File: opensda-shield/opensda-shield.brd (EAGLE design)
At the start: 21.6 x 53.3 mm, 17 parts, among them IC1 74LVC125, IC2 74LVC125, J1 61302011121, J2 61302011121, J3 61300211121, J4 CORTEX_DEBUG_PTH, J5 61301511121

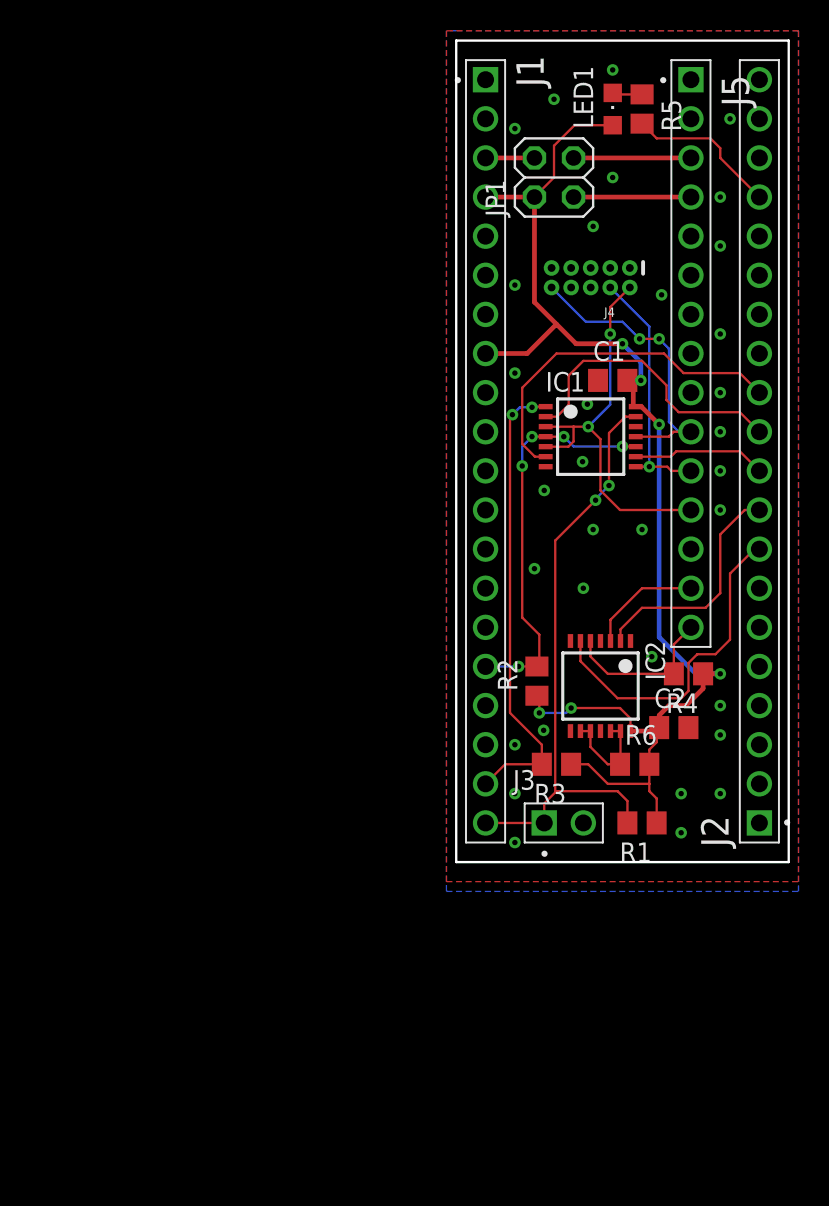
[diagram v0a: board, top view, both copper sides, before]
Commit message: Premisten J4 a prehozeny gaty bufferu
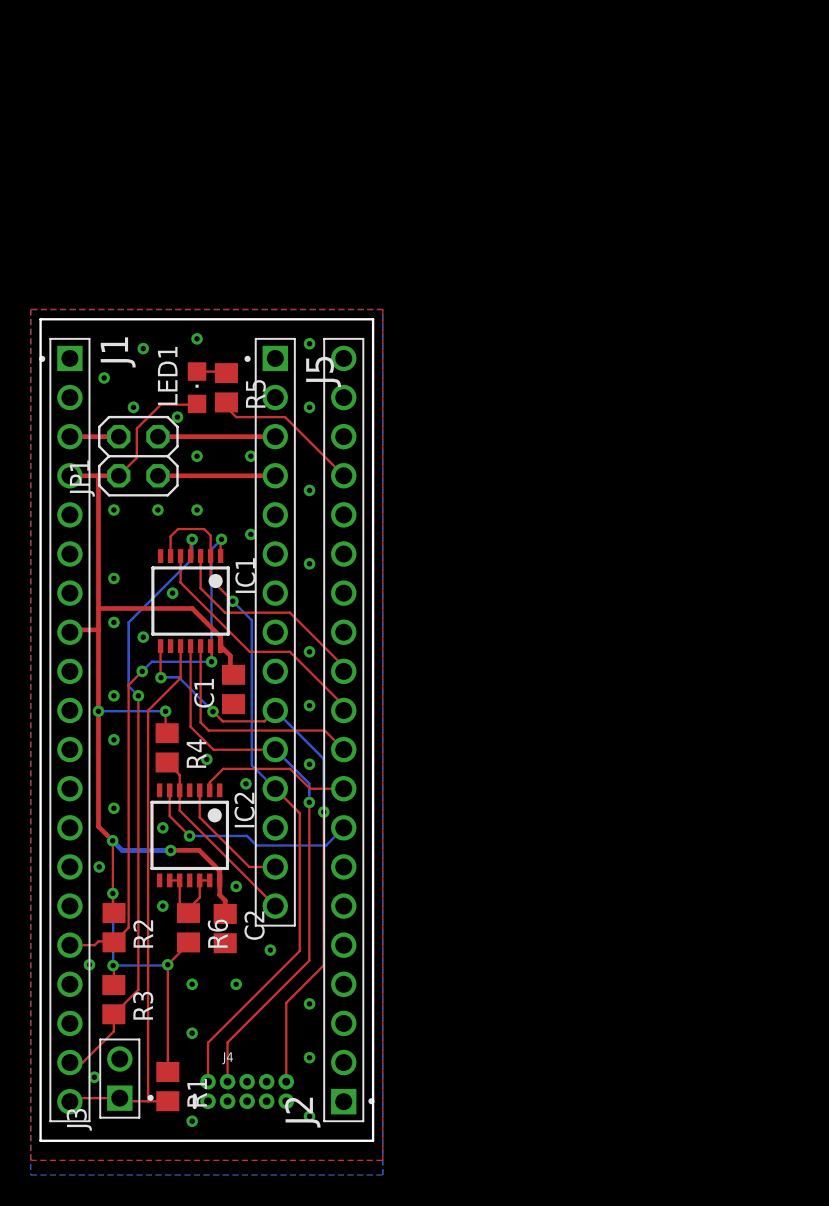
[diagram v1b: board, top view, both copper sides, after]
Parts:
- moved J4 57.4 mm to (16.3, 6.69), turned to 0 degrees
- moved R1 35.2 mm to (11.1, 7.01), turned to 270 degrees
- moved R4 34.2 mm to (11.1, 29.0), turned to 270 degrees
- moved J3 33.3 mm to (8.00, 7.53), turned to 90 degrees
- moved R3 32.6 mm to (7.61, 12.7), turned to 270 degrees
- moved J1 32.5 mm to (4.76, 30.2)
- moved J2 32.5 mm to (22.5, 30.2)
- moved J5 32.5 mm to (18.1, 36.5)
- moved JP1 32.5 mm to (9.21, 47.9)
- moved LED1 32.5 mm to (13.0, 52.4)
- moved R5 32.5 mm to (14.9, 52.4)
- moved C2 31.9 mm to (14.8, 17.3), turned to 270 degrees
- moved R2 31.8 mm to (7.63, 17.3), turned to 270 degrees
- moved C1 31.8 mm to (15.4, 32.8), turned to 90 degrees
- moved R6 30.9 mm to (12.5, 17.3), turned to 270 degrees
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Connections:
- net GND: now also IC1.9; no longer IC1.12
- net PTA4: now also IC1.1, IC1.13; no longer IC1.10, IC1.4
- net PTB0: now also IC1.4; no longer IC1.1
- net PTB1: now also IC1.10; no longer IC1.13
- net PTC5: now also IC1.12; no longer IC1.9
- net PTC6: now also IC1.5; no longer IC1.2
- net PTC7: now also IC1.3; no longer IC1.6
- net RST_TGT: now also IC1.8; no longer IC1.11
- net SWD_CLK_TGT: now also IC1.11; no longer IC1.8
- net SWD_DIO_TGT: now also IC1.2, IC1.6; no longer IC1.3, IC1.5
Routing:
- net SWD_CLK_TGT: track 16.4 -> 36.0 mm
- net RST_TGT: track 19.4 -> 37.4 mm, vias 2 -> 3
- net SWD_DIO_TGT: track 27.0 -> 44.6 mm, vias 2 -> 1
- net PTA4: track 26.1 -> 36.5 mm, vias 5 -> 3
- net PTB0: track 30.2 -> 39.5 mm
- net PTC7: track 22.9 -> 13.8 mm
- net PTC3: track 21.5 -> 14.2 mm, vias 0 -> 1
- net PTC5: track 8.70 -> 15.0 mm
- net PTC4: track 15.2 -> 10.1 mm
- net PTC6: track 19.0 -> 15.9 mm
- net 3V3: track 85.7 -> 88.6 mm, vias 6 -> 7
- net PTB1: track 39.5 -> 37.0 mm, vias 2 -> 0
- net TX_TGT: track 10.4 -> 12.2 mm
- net N$5: track 6.88 -> 6.11 mm
- net RX_TGT: track 7.45 -> 8.00 mm

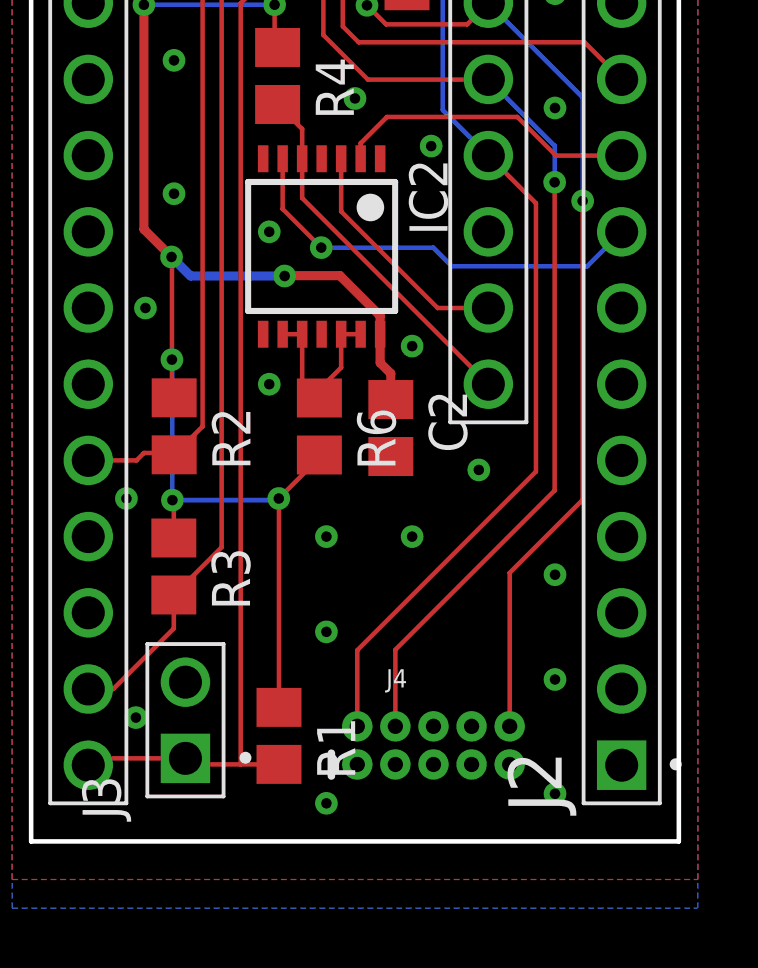
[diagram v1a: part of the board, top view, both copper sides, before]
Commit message: Posunuti J4
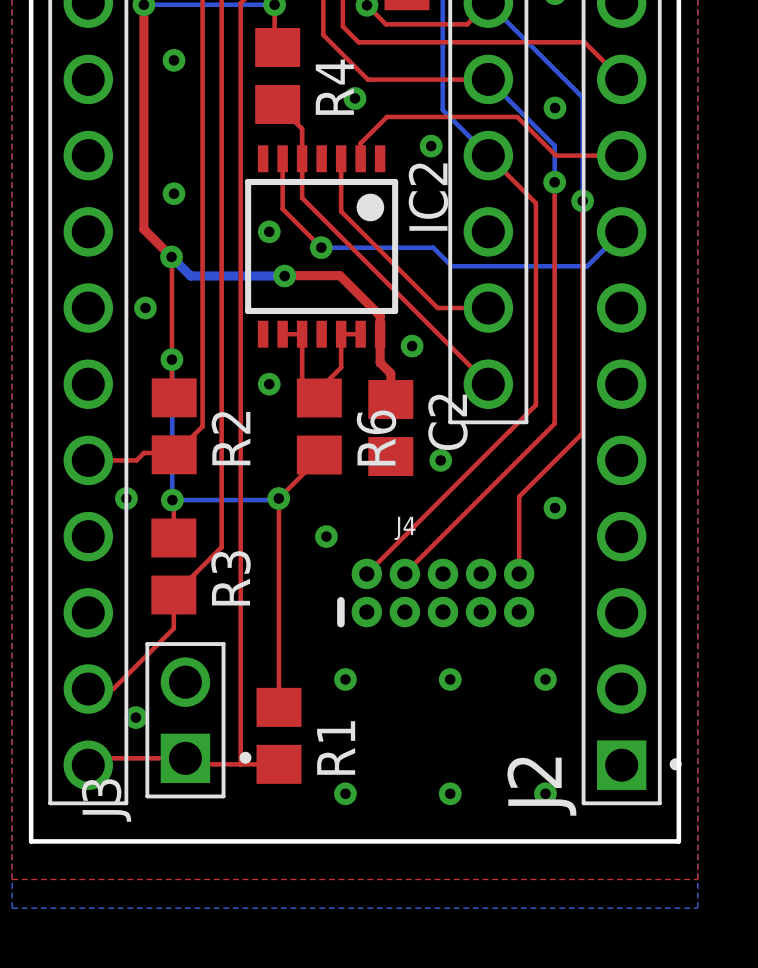
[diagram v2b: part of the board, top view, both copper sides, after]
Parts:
- moved J4 5.09 mm to (16.6, 11.8)
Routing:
- net SWD_CLK_TGT: track 36.0 -> 30.8 mm
- net RST_TGT: track 37.4 -> 32.2 mm
- net SWD_DIO_TGT: track 44.6 -> 39.4 mm
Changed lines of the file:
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@@
 <attribute name="VALUE" x="11.684" y="4.2291" size="1.27" layer="27" rot="R90"/>
 </element>
-<element name="J4" library="SparkFun-Connectors" library_urn="urn:adsk.eagle:library:513" package="2X5-PTH-1.27MM" package3d_urn="urn:adsk.eagle:package:38290/1" value="CORTEX_DEBUG_PTH" x="16.2687" y="6.6929" smashed="yes">
-<attribute name="NAME" x="14.6939" y="8.6233" size="0.6096" layer="25" font="vector" ratio="20"/>
-<attribute name="VALUE" x="14.4399" y="4.2291" size="0.6096" layer="27" font="vector" ratio="20"/>
+<element name="J4" library="SparkFun-Connectors" library_urn="urn:adsk.eagle:library:513" package="2X5-PTH-1.27MM" package3d_urn="urn:adsk.eagle:package:38290/1" value="CORTEX_DEBUG_PTH" x="16.5862" y="11.7729" smashed="yes">
+<attribute name="NAME" x="15.0114" y="13.7033" size="0.6096" layer="25" font="vector" ratio="20"/>
+<attribute name="VALUE" x="14.7574" y="9.3091" size="0.6096" layer="27" font="vector" ratio="20"/>
 </element>
 <element name="J5" library="Headers" library_urn="urn:adsk.eagle:library:11687645" package="61301511121" package3d_urn="urn:adsk.eagle:package:11391913/2" value="61301511121" x="18.0975" y="36.5125" smashed="yes" rot="R270">
@@
 <contactref element="IC1" pad="9"/>
 <via x="12.7" y="13.6525" extent="1-16" drill="0.35"/>
-<via x="17.78" y="15.875" extent="1-16" drill="0.35"/>
-<via x="15.5575" y="13.6525" extent="1-16" drill="0.35"/>
-<via x="12.7" y="10.4775" extent="1-16" drill="0.35"/>
-<via x="20.32" y="12.3825" extent="1-16" drill="0.35"/>
-<via x="20.32" y="8.89" extent="1-16" drill="0.35"/>
-<via x="20.32" y="5.08" extent="1-16" drill="0.35"/>
-<via x="12.7" y="4.7625" extent="1-16" drill="0.35"/>
+<via x="16.51" y="16.1925" extent="1-16" drill="0.35"/>
+<via x="16.8275" y="8.89" extent="1-16" drill="0.35"/>
+<via x="13.335" y="8.89" extent="1-16" drill="0.35"/>
+<via x="20.0025" y="5.08" extent="1-16" drill="0.35"/>
+<via x="20.0025" y="8.89" extent="1-16" drill="0.35"/>
+<via x="16.8275" y="5.08" extent="1-16" drill="0.35"/>
+<via x="13.335" y="5.08" extent="1-16" drill="0.35"/>
 <via x="6.35" y="7.62" extent="1-16" drill="0.35"/>
 <via x="6.0325" y="14.9225" extent="1-16" drill="0.35"/>
@@
 <via x="10.795" y="23.8125" extent="1-16" drill="0.35"/>
 <via x="10.795" y="18.7325" extent="1-16" drill="0.35"/>
+<via x="20.32" y="14.605" extent="1-16" drill="0.35"/>
 </signal>
 <signal name="VIN">
@@
 <wire x1="16.57985" y1="27.87015" x2="18.0975" y2="26.3525" width="0.1524" layer="16"/>
 <wire x1="16.57985" y1="37.2872" x2="16.57985" y2="27.87015" width="0.1524" layer="16"/>
-<wire x1="13.7287" y1="7.3279" x2="13.7287" y2="9.86155" width="0.1524" layer="1"/>
+<wire x1="18.81505" y1="17.1704" x2="18.8087" y2="17.1704" width="0.1524" layer="1"/>
+<wire x1="18.8087" y1="17.1704" x2="14.0462" y2="12.4079" width="0.1524" layer="1"/>
 <wire x1="19.685" y1="24.765" x2="18.0975" y2="26.3525" width="0.1524" layer="1"/>
-<wire x1="13.7287" y1="9.86155" x2="19.685" y2="15.81785" width="0.1524" layer="1"/>
-<wire x1="19.685" y1="15.81785" x2="19.685" y2="24.765" width="0.1524" layer="1"/>
+<wire x1="18.81505" y1="17.1704" x2="19.685" y2="18.04035" width="0.1524" layer="1"/>
+<wire x1="19.685" y1="18.04035" x2="19.685" y2="24.765" width="0.1524" layer="1"/>
 <wire x1="13.48105" y1="43.21175" x2="11.77925" y2="43.21175" width="0.1524" layer="1"/>
 <wire x1="11.2984" y1="42.7309" x2="11.2984" y2="41.46315" width="0.1524" layer="1"/>
@@
 <wire x1="18.09115" y1="28.88615" x2="14.0843" y2="28.88615" width="0.1524" layer="1"/>
 <wire x1="12.5984" y1="30.37205" x2="14.0843" y2="28.88615" width="0.1524" layer="1"/>
-<wire x1="14.9987" y1="7.3279" x2="14.9987" y2="9.8806" width="0.1524" layer="1"/>
-<wire x1="20.3073" y1="15.1892" x2="20.3073" y2="25.4635" width="0.1524" layer="1"/>
+<wire x1="20.3073" y1="17.4117" x2="20.3073" y2="25.4635" width="0.1524" layer="1"/>
 <via x="20.3073" y="25.4635" extent="1-16" drill="0.35"/>
 <wire x1="20.3073" y1="25.4635" x2="20.3073" y2="26.6827" width="0.1524" layer="16"/>
 <wire x1="20.3073" y1="26.6827" x2="18.0975" y2="28.8925" width="0.1524" layer="16"/>
-<wire x1="14.9987" y1="9.8806" x2="20.3073" y2="15.1892" width="0.1524" layer="1"/>
+<wire x1="15.3162" y1="12.4079" x2="15.3162" y2="12.4206" width="0.1524" layer="1"/>
+<wire x1="20.3073" y1="17.4117" x2="15.3162" y2="12.4206" width="0.1524" layer="1"/>
 </signal>
 <signal name="RST_TGT">
@@
 <wire x1="14.68755" y1="30.72765" x2="14.05255" y2="31.36265" width="0.1524" layer="1"/>
 <wire x1="17.39265" y1="30.72765" x2="14.68755" y2="30.72765" width="0.1524" layer="1"/>
-<wire x1="18.8087" y1="7.3279" x2="18.8087" y2="12.446" width="0.1524" layer="1"/>
-<wire x1="21.24075" y1="14.87805" x2="21.24075" y2="24.8412" width="0.1524" layer="1"/>
+<wire x1="19.1262" y1="12.4079" x2="19.1262" y2="14.986" width="0.1524" layer="1"/>
+<wire x1="21.24075" y1="17.10055" x2="21.24075" y2="24.8412" width="0.1524" layer="1"/>
 <via x="21.24075" y="24.8412" extent="1-16" drill="0.35"/>
 <wire x1="21.24075" y1="24.8412" x2="21.24075" y2="28.28925" width="0.1524" layer="16"/>
 <wire x1="21.24075" y1="28.28925" x2="18.0975" y2="31.4325" width="0.1524" layer="16"/>
-<wire x1="18.8087" y1="12.446" x2="21.24075" y2="14.87805" width="0.1524" layer="1"/>
+<wire x1="19.1262" y1="14.986" x2="21.24075" y2="17.10055" width="0.1524" layer="1"/>
 </signal>
 <signal name="RX_TGT">

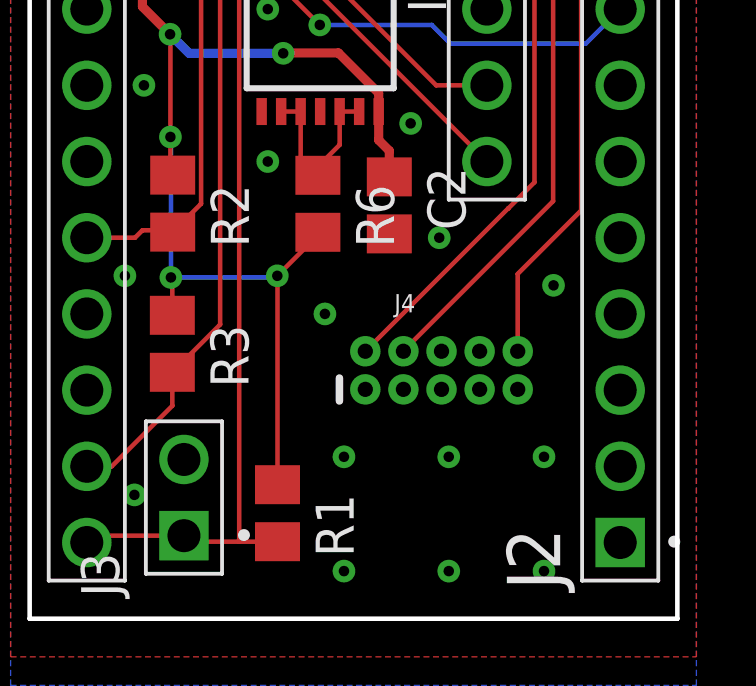
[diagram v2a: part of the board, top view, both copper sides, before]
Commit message: Posunuti J4
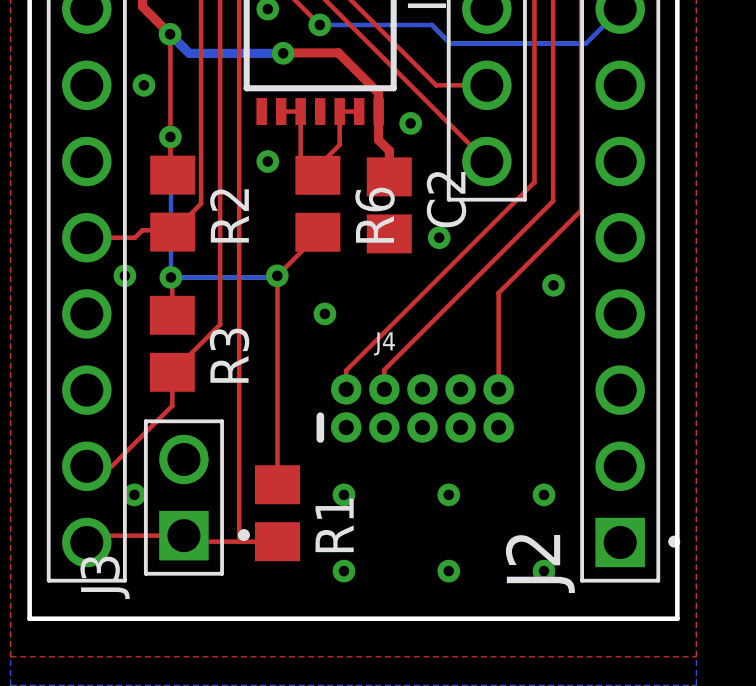
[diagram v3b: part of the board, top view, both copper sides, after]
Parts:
- moved J4 1.42 mm to (16.0, 10.5)
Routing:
- net SWD_CLK_TGT: track 30.8 -> 32.4 mm
- net RST_TGT: track 32.2 -> 33.7 mm
- net SWD_DIO_TGT: track 39.4 -> 40.9 mm
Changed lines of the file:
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@@
 <attribute name="VALUE" x="11.684" y="4.2291" size="1.27" layer="27" rot="R90"/>
 </element>
-<element name="J4" library="SparkFun-Connectors" library_urn="urn:adsk.eagle:library:513" package="2X5-PTH-1.27MM" package3d_urn="urn:adsk.eagle:package:38290/1" value="CORTEX_DEBUG_PTH" x="16.5862" y="11.7729" smashed="yes">
-<attribute name="NAME" x="15.0114" y="13.7033" size="0.6096" layer="25" font="vector" ratio="20"/>
-<attribute name="VALUE" x="14.7574" y="9.3091" size="0.6096" layer="27" font="vector" ratio="20"/>
+<element name="J4" library="SparkFun-Connectors" library_urn="urn:adsk.eagle:library:513" package="2X5-PTH-1.27MM" package3d_urn="urn:adsk.eagle:package:38290/1" value="CORTEX_DEBUG_PTH" x="15.9512" y="10.5029" smashed="yes">
+<attribute name="NAME" x="14.3764" y="12.4333" size="0.6096" layer="25" font="vector" ratio="20"/>
+<attribute name="VALUE" x="14.1224" y="8.0391" size="0.6096" layer="27" font="vector" ratio="20"/>
 </element>
 <element name="J5" library="Headers" library_urn="urn:adsk.eagle:library:11687645" package="61301511121" package3d_urn="urn:adsk.eagle:package:11391913/2" value="61301511121" x="18.0975" y="36.5125" smashed="yes" rot="R270">
@@
 <via x="12.7" y="13.6525" extent="1-16" drill="0.35"/>
 <via x="16.51" y="16.1925" extent="1-16" drill="0.35"/>
-<via x="16.8275" y="8.89" extent="1-16" drill="0.35"/>
-<via x="13.335" y="8.89" extent="1-16" drill="0.35"/>
+<via x="16.8275" y="7.62" extent="1-16" drill="0.35"/>
+<via x="13.335" y="7.62" extent="1-16" drill="0.35"/>
 <via x="20.0025" y="5.08" extent="1-16" drill="0.35"/>
-<via x="20.0025" y="8.89" extent="1-16" drill="0.35"/>
+<via x="20.0025" y="7.62" extent="1-16" drill="0.35"/>
 <via x="16.8275" y="5.08" extent="1-16" drill="0.35"/>
 <via x="13.335" y="5.08" extent="1-16" drill="0.35"/>
@@
 <wire x1="16.57985" y1="27.87015" x2="18.0975" y2="26.3525" width="0.1524" layer="16"/>
 <wire x1="16.57985" y1="37.2872" x2="16.57985" y2="27.87015" width="0.1524" layer="16"/>
-<wire x1="18.81505" y1="17.1704" x2="18.8087" y2="17.1704" width="0.1524" layer="1"/>
-<wire x1="18.8087" y1="17.1704" x2="14.0462" y2="12.4079" width="0.1524" layer="1"/>
+<wire x1="13.4112" y1="11.1379" x2="13.4112" y2="11.76655" width="0.1524" layer="1"/>
+<wire x1="19.685" y1="18.04035" x2="13.4112" y2="11.76655" width="0.1524" layer="1"/>
 <wire x1="19.685" y1="24.765" x2="18.0975" y2="26.3525" width="0.1524" layer="1"/>
-<wire x1="18.81505" y1="17.1704" x2="19.685" y2="18.04035" width="0.1524" layer="1"/>
 <wire x1="19.685" y1="18.04035" x2="19.685" y2="24.765" width="0.1524" layer="1"/>
 <wire x1="13.48105" y1="43.21175" x2="11.77925" y2="43.21175" width="0.1524" layer="1"/>
@@
 <wire x1="20.3073" y1="25.4635" x2="20.3073" y2="26.6827" width="0.1524" layer="16"/>
 <wire x1="20.3073" y1="26.6827" x2="18.0975" y2="28.8925" width="0.1524" layer="16"/>
-<wire x1="15.3162" y1="12.4079" x2="15.3162" y2="12.4206" width="0.1524" layer="1"/>
-<wire x1="20.3073" y1="17.4117" x2="15.3162" y2="12.4206" width="0.1524" layer="1"/>
+<wire x1="14.6812" y1="11.1379" x2="14.6812" y2="11.7856" width="0.1524" layer="1"/>
+<wire x1="20.3073" y1="17.4117" x2="14.6812" y2="11.7856" width="0.1524" layer="1"/>
 </signal>
 <signal name="RST_TGT">
@@
 <wire x1="14.68755" y1="30.72765" x2="14.05255" y2="31.36265" width="0.1524" layer="1"/>
 <wire x1="17.39265" y1="30.72765" x2="14.68755" y2="30.72765" width="0.1524" layer="1"/>
-<wire x1="19.1262" y1="12.4079" x2="19.1262" y2="14.986" width="0.1524" layer="1"/>
+<wire x1="18.4912" y1="11.1379" x2="18.4912" y2="14.351" width="0.1524" layer="1"/>
 <wire x1="21.24075" y1="17.10055" x2="21.24075" y2="24.8412" width="0.1524" layer="1"/>
 <via x="21.24075" y="24.8412" extent="1-16" drill="0.35"/>
 <wire x1="21.24075" y1="24.8412" x2="21.24075" y2="28.28925" width="0.1524" layer="16"/>
 <wire x1="21.24075" y1="28.28925" x2="18.0975" y2="31.4325" width="0.1524" layer="16"/>
-<wire x1="19.1262" y1="14.986" x2="21.24075" y2="17.10055" width="0.1524" layer="1"/>
+<wire x1="18.4912" y1="14.351" x2="21.24075" y2="17.10055" width="0.1524" layer="1"/>
 </signal>
 <signal name="RX_TGT">

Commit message: Pridany popisky
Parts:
- moved C1 4.25 mm to (15.4, 37.1), turned to 270 degrees
- moved LED1 4.14 mm to (8.89, 52.7)
- moved R5 4.14 mm to (10.8, 52.7)
- moved C2 1.27 mm to (13.6, 17.3)
- moved IC1 0.95 mm to (11.6, 38.5)
- moved IC2 0.95 mm to (11.6, 23.3)
- moved R6 0.95 mm to (11.5, 17.3)
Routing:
- net PTD4: track 9.78 -> 13.9 mm
- net SWD_DIO_TGT: track 40.9 -> 44.7 mm
- net 3V3: track 88.6 -> 85.0 mm
- net PTC7: track 13.8 -> 15.6 mm
- net PTC6: track 15.9 -> 17.6 mm
- net PTC4: track 10.1 -> 11.3 mm
- net RST_TGT: track 33.7 -> 34.3 mm
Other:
- outline, holes or cut-outs redrawn
- board text added: "3V3"
- board text added: "5V"
- board text added: "CLK"
- board text added: "DIO"
- board text added: "GND"
- board text added: "PTB1"
- board text added: "PTD4"
- board text added: "RST"
- board text added: "RX"
- board text added: "TX"
